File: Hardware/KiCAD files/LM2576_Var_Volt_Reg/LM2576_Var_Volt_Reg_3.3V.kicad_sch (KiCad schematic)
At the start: 13 parts, among them J1 Conn_01x03_Pin, U2 LM2576HVS-ADJ

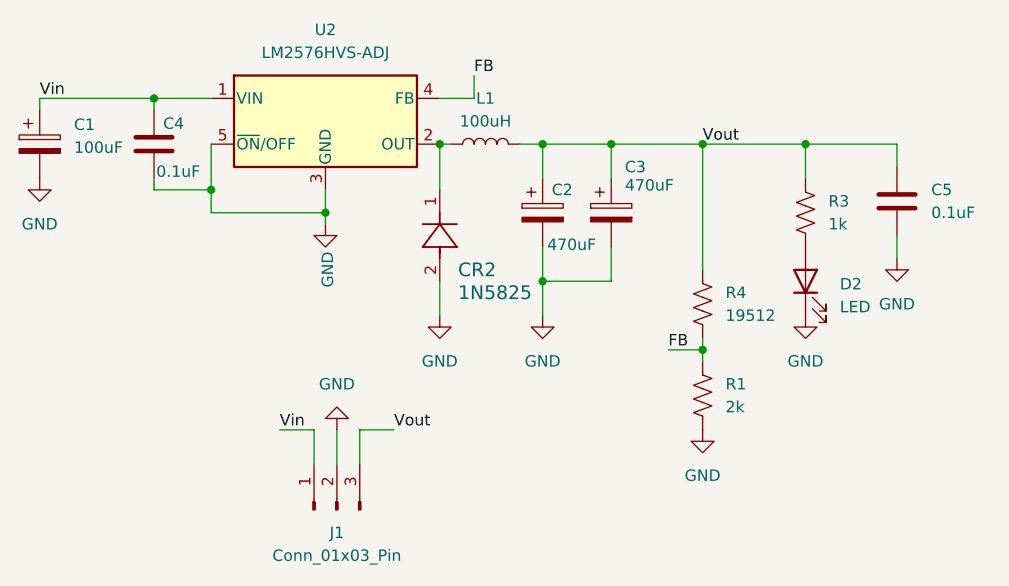
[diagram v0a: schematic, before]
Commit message: general updates to the schematics and layouts
includes some backchecks tot he master schematic to be accurate for the paper
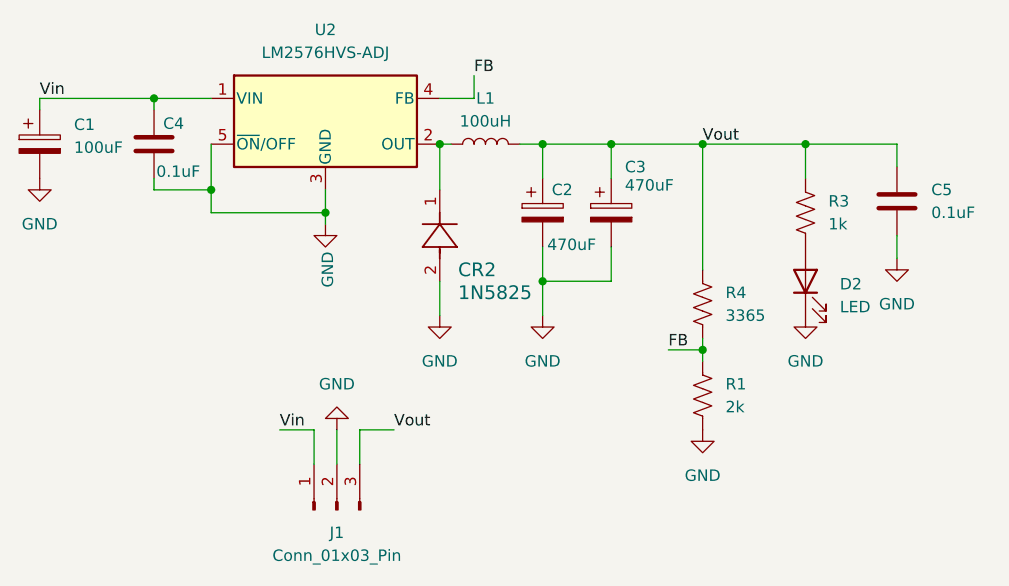
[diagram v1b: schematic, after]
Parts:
- R4: value 19512 -> 3365
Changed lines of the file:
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@@
 			)
 		)
-		(property "Value" "19512"
+		(property "Value" "3365"
 			(at 165.1 81.2799 0)
 			(show_name no)

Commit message: V2 mainboard
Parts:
- R1: value 2k -> 1k
- R4: value 3365 -> 1682
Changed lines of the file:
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@@
 		)
 		(instances
-			(project "LM2576_Var_Volt_Reg"
+			(project "LM2576_Var_Volt_Reg_3.3V"
 				(path "/05ad55a9-73a4-4419-8d6d-9b068d5aca56"
 					(reference "D2")
@@
 		)
 		(instances
-			(project "LM2576_Var_Volt_Reg"
+			(project "LM2576_Var_Volt_Reg_3.3V"
 				(path "/05ad55a9-73a4-4419-8d6d-9b068d5aca56"
 					(reference "#PWR05")
@@
 		)
 		(instances
-			(project "LM2576_Var_Volt_Reg"
+			(project "LM2576_Var_Volt_Reg_3.3V"
 				(path "/05ad55a9-73a4-4419-8d6d-9b068d5aca56"
 					(reference "#PWR08")
@@
 		)
 		(instances
-			(project "LM2576_Var_Volt_Reg"
+			(project "LM2576_Var_Volt_Reg_3.3V"
 				(path "/05ad55a9-73a4-4419-8d6d-9b068d5aca56"
 					(reference "#PWR01")
@@
 		)
 		(instances
-			(project "LM2576_Var_Volt_Reg"
+			(project "LM2576_Var_Volt_Reg_3.3V"
 				(path "/05ad55a9-73a4-4419-8d6d-9b068d5aca56"
 					(reference "L1")
@@
 			)
 		)
-		(property "Value" "3365"
+		(property "Value" "1682"
 			(at 165.1 81.2799 0)
 			(show_name no)
@@
 		)
 		(instances
-			(project "LM2576_Var_Volt_Reg"
+			(project "LM2576_Var_Volt_Reg_3.3V"
 				(path "/05ad55a9-73a4-4419-8d6d-9b068d5aca56"
 					(reference "R4")
@@
 		)
 		(instances
-			(project "LM2576_Var_Volt_Reg"
+			(project "LM2576_Var_Volt_Reg_3.3V"
 				(path "/05ad55a9-73a4-4419-8d6d-9b068d5aca56"
 					(reference "#PWR07")
@@
 		)
 		(instances
-			(project "LM2576_Var_Volt_Reg"
+			(project "LM2576_Var_Volt_Reg_3.3V"
 				(path "/05ad55a9-73a4-4419-8d6d-9b068d5aca56"
 					(reference "#PWR03")
@@
 			)
 		)
-		(property "Value" "2k"
+		(property "Value" "1k"
 			(at 165.1 91.4399 0)
 			(show_name no)
@@
 		)
 		(instances
-			(project "LM2576_Var_Volt_Reg"
+			(project "LM2576_Var_Volt_Reg_3.3V"
 				(path "/05ad55a9-73a4-4419-8d6d-9b068d5aca56"
 					(reference "R1")
@@
 		)
 		(instances
-			(project "LM2576_Var_Volt_Reg"
+			(project "LM2576_Var_Volt_Reg_3.3V"
 				(path "/05ad55a9-73a4-4419-8d6d-9b068d5aca56"
 					(reference "#PWR04")
@@
 		)
 		(instances
-			(project "LM2576_Var_Volt_Reg"
+			(project "LM2576_Var_Volt_Reg_3.3V"
 				(path "/05ad55a9-73a4-4419-8d6d-9b068d5aca56"
 					(reference "C1")
@@
 		)
 		(instances
-			(project "LM2576_Var_Volt_Reg"
+			(project "LM2576_Var_Volt_Reg_3.3V"
 				(path "/05ad55a9-73a4-4419-8d6d-9b068d5aca56"
 					(reference "C3")
@@
 		)
 		(instances
-			(project "LM2576_Var_Volt_Reg"
+			(project "LM2576_Var_Volt_Reg_3.3V"
 				(path "/05ad55a9-73a4-4419-8d6d-9b068d5aca56"
 					(reference "C5")
@@
 		)
 		(instances
-			(project "LM2576_Var_Volt_Reg"
+			(project "LM2576_Var_Volt_Reg_3.3V"
 				(path "/05ad55a9-73a4-4419-8d6d-9b068d5aca56"
 					(reference "#PWR02")
@@
 		)
 		(instances
-			(project "LM2576_Var_Volt_Reg"
+			(project "LM2576_Var_Volt_Reg_3.3V"
 				(path "/05ad55a9-73a4-4419-8d6d-9b068d5aca56"
 					(reference "U2")
@@
 		)
 		(instances
-			(project "LM2576_Var_Volt_Reg"
+			(project "LM2576_Var_Volt_Reg_3.3V"
 				(path "/05ad55a9-73a4-4419-8d6d-9b068d5aca56"
 					(reference "J1")
@@
 		)
 		(instances
-			(project "LM2576_Var_Volt_Reg"
+			(project "LM2576_Var_Volt_Reg_3.3V"
 				(path "/05ad55a9-73a4-4419-8d6d-9b068d5aca56"
 					(reference "#PWR06")
@@
 		)
 		(instances
-			(project "LM2576_Var_Volt_Reg"
+			(project "LM2576_Var_Volt_Reg_3.3V"
 				(path "/05ad55a9-73a4-4419-8d6d-9b068d5aca56"
 					(reference "C2")
@@
 		)
 		(instances
-			(project "LM2576_Var_Volt_Reg"
+			(project "LM2576_Var_Volt_Reg_3.3V"
 				(path "/05ad55a9-73a4-4419-8d6d-9b068d5aca56"
 					(reference "R3")
@@
 		)
 		(instances
-			(project "LM2576_Var_Volt_Reg"
+			(project "LM2576_Var_Volt_Reg_3.3V"
 				(path "/05ad55a9-73a4-4419-8d6d-9b068d5aca56"
 					(reference "C4")
@@
 		)
 		(instances
-			(project "LM2576_Var_Volt_Reg"
+			(project "LM2576_Var_Volt_Reg_3.3V"
 				(path "/05ad55a9-73a4-4419-8d6d-9b068d5aca56"
 					(reference "CR2")
